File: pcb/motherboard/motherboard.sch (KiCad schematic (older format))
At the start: 37 parts, among them J1 -, J10 PSU, J11 RESET-SW, J14 EXT, J15 EXT-PW, J16 EXT-I2C, J6 PSU-SIG, J7 ICSP-1, J8 FRONT PANEL, SW1 RESET, U1 ATMEGA2560-16AU, Y2 16.00 MHz

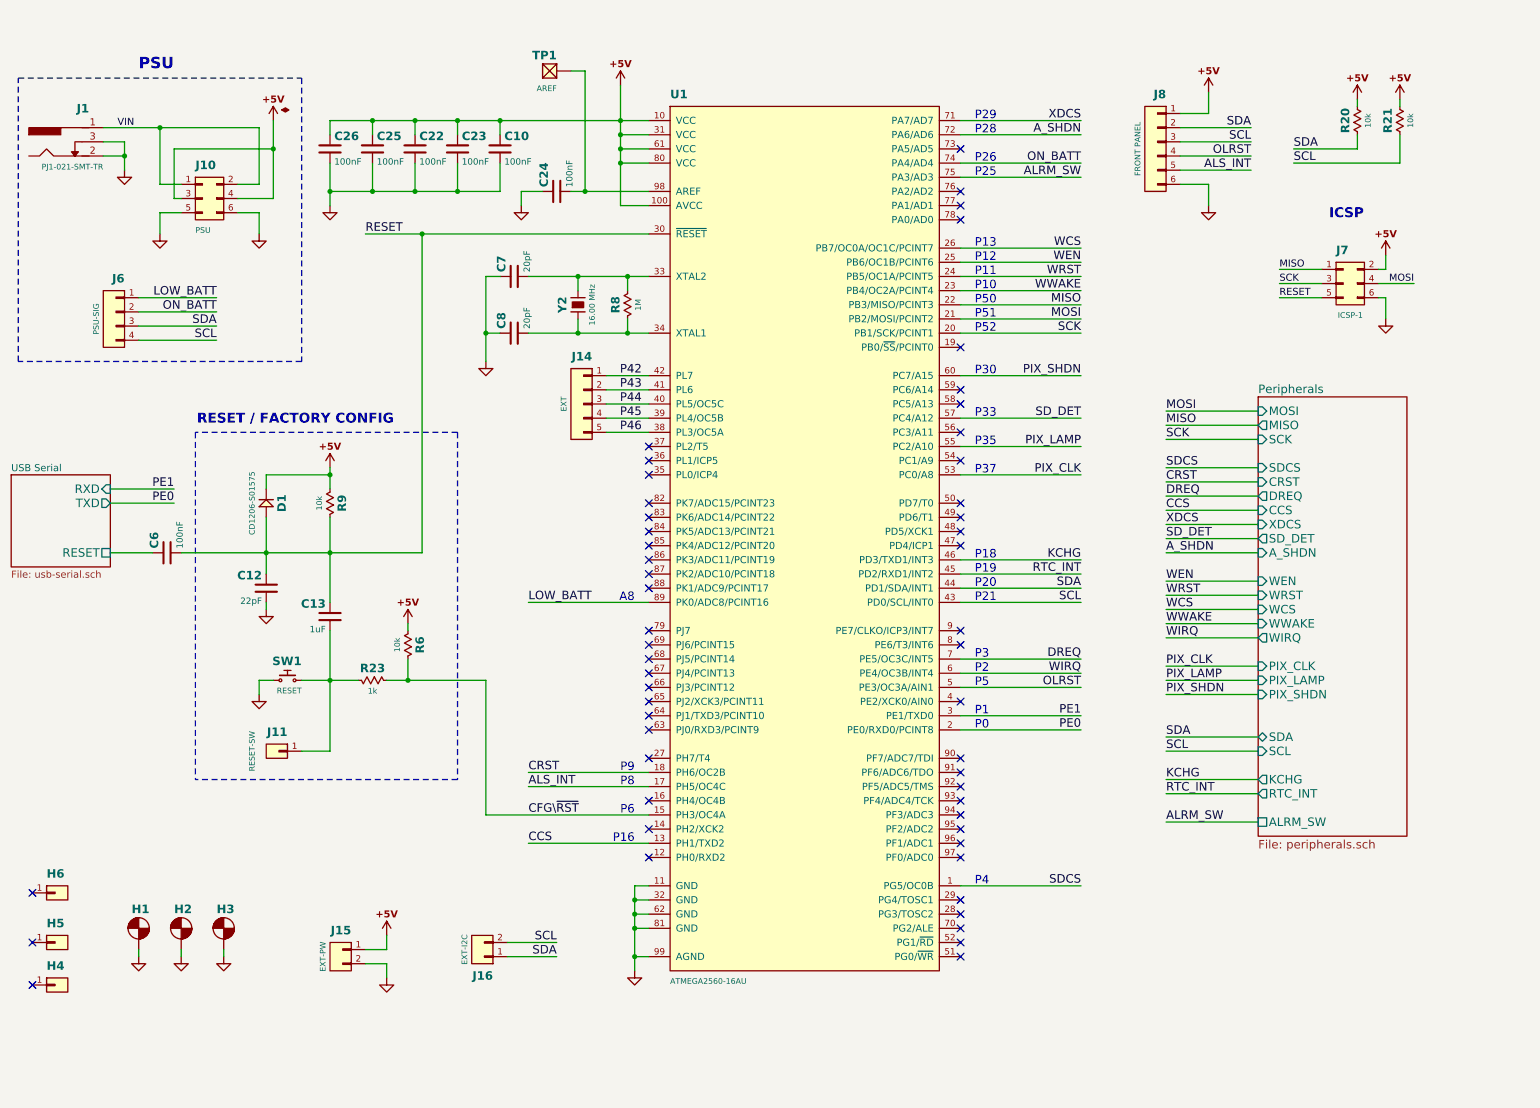
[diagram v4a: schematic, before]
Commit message: Replaced battery holder for Harwin S8411-45R
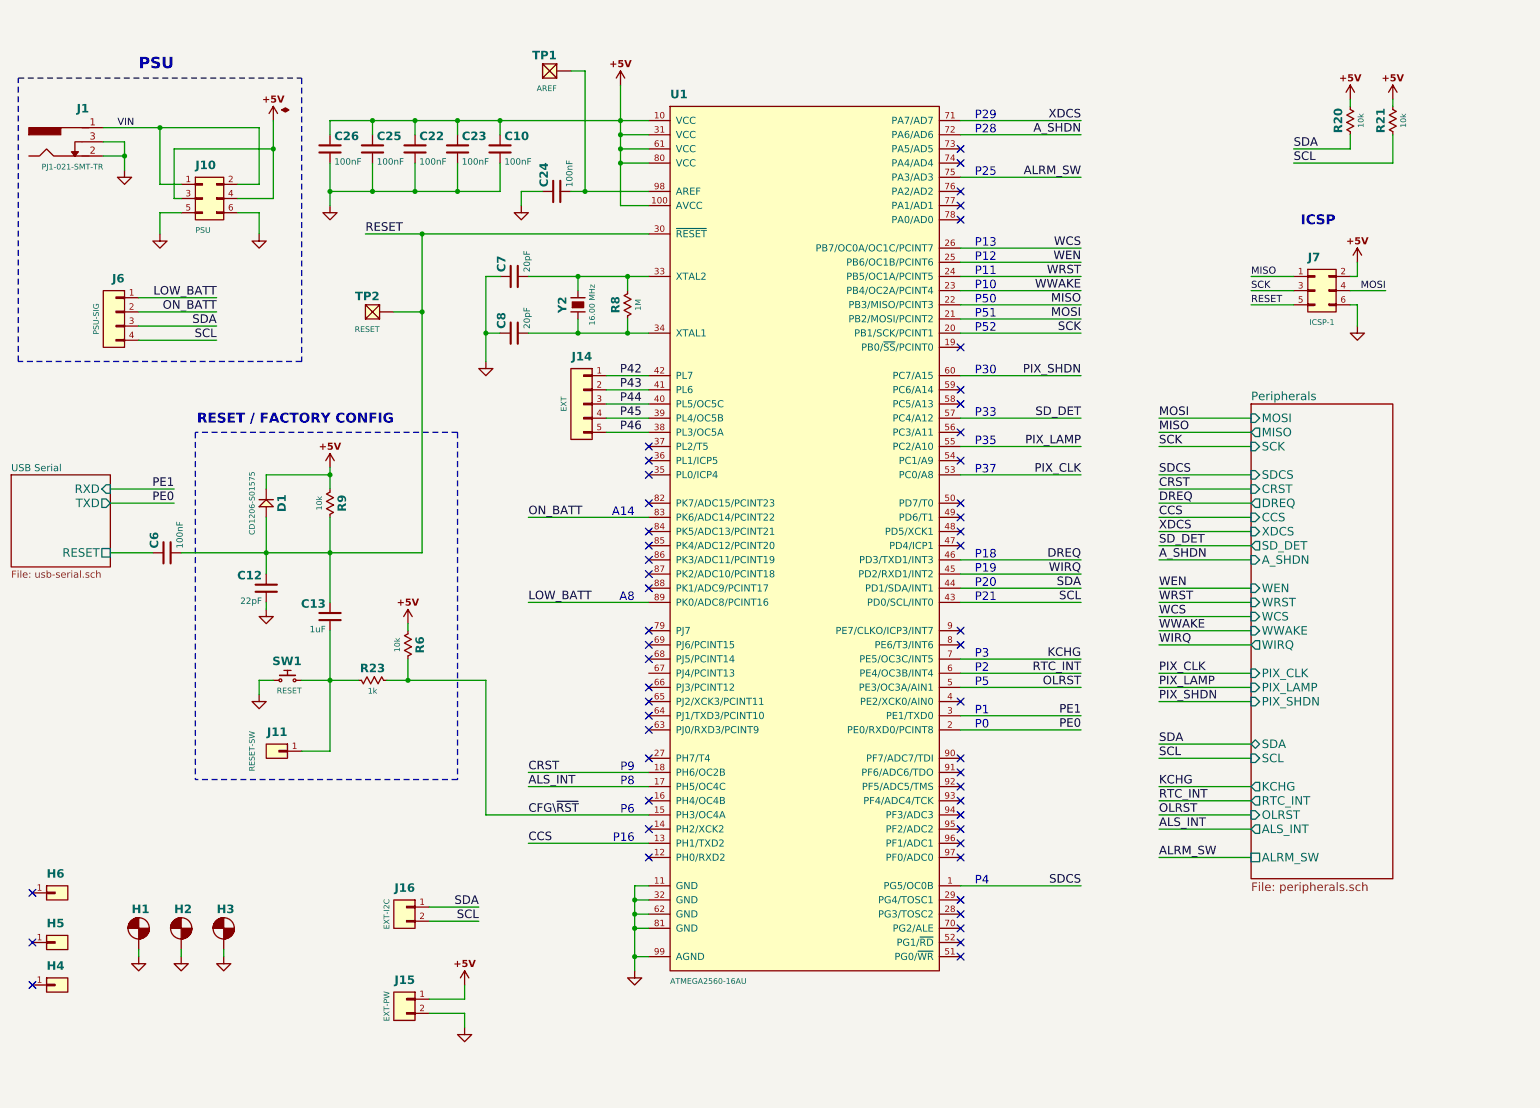
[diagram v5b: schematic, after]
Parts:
- removed J8: FRONT PANEL, conn-wire-pads:WP-50mil-1x06, symbol connectors:HEADER-1x06
- added TP2: RESET, conn-wire-pads:TEST-POINT-50, symbol connectors:TEST-POINT
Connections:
- net DREQ: now also U1.46 (PD3/TXD1/INT3); no longer U1.7 (PE5/OC3C/INT5)
- net KCHG: now also U1.7 (PE5/OC3C/INT5); no longer U1.46 (PD3/TXD1/INT3)
- net ON_BATT: now also U1.83 (PK6/ADC14/PCINT22); no longer U1.74 (PA4/AD4)
- net RESET: now also TP2.1 (P1)
- net RTC_INT: now also U1.6 (PE4/OC3B/INT4); no longer U1.45 (PD2/RXD1/INT2)
- net WIRQ: now also U1.45 (PD2/RXD1/INT2); no longer U1.6 (PE4/OC3B/INT4)
- no-connect marks 54 -> 53
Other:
- note added: "A14"
- note removed: "P26"
- moved on the sheet: J15, J16, J7, R20, R21

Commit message: Fix: Wrong footprint for R20-22 and C14
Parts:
- J7: value ICSP-1 -> ICSP
- R20, R21: footprint smt:C-0603 -> smt:R-0603
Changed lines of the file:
@@
 P 9800 2450
 F 0 "J7" H 9700 2650 60  0000 L BNB
-F 1 "ICSP-1" H 9800 2250 40  0000 C TNN
+F 1 "ICSP" H 9800 2250 40  0000 C TNN
 F 2 "conn-header:HDR-M-2x03" H 9800 1250 60  0001 C CNN
 F 3 "" H 9800 1250 60  0001 C CNN
@@
 F 0 "R20" H 10000 1335 60  0000 C CNB
 F 1 "10k" H 10000 1175 40  0000 C CNN
-F 2 "smt:C-0603" H 10000 1110 40  0001 C CNN
+F 2 "smt:R-0603" H 10000 1110 40  0001 C CNN
 F 3 "" H 10000 1350 60  0000 C CNN
 F 4 "-" H 10000 1410 45  0001 C CNN "Part"
@@
 F 0 "R21" H 10300 1335 60  0000 C CNB
 F 1 "10k" H 10300 1175 40  0000 C CNN
-F 2 "smt:C-0603" H 10300 1110 40  0001 C CNN
+F 2 "smt:R-0603" H 10300 1110 40  0001 C CNN
 F 3 "" H 10300 1350 60  0000 C CNN
 F 4 "-" H 10300 1410 45  0001 C CNN "Part"

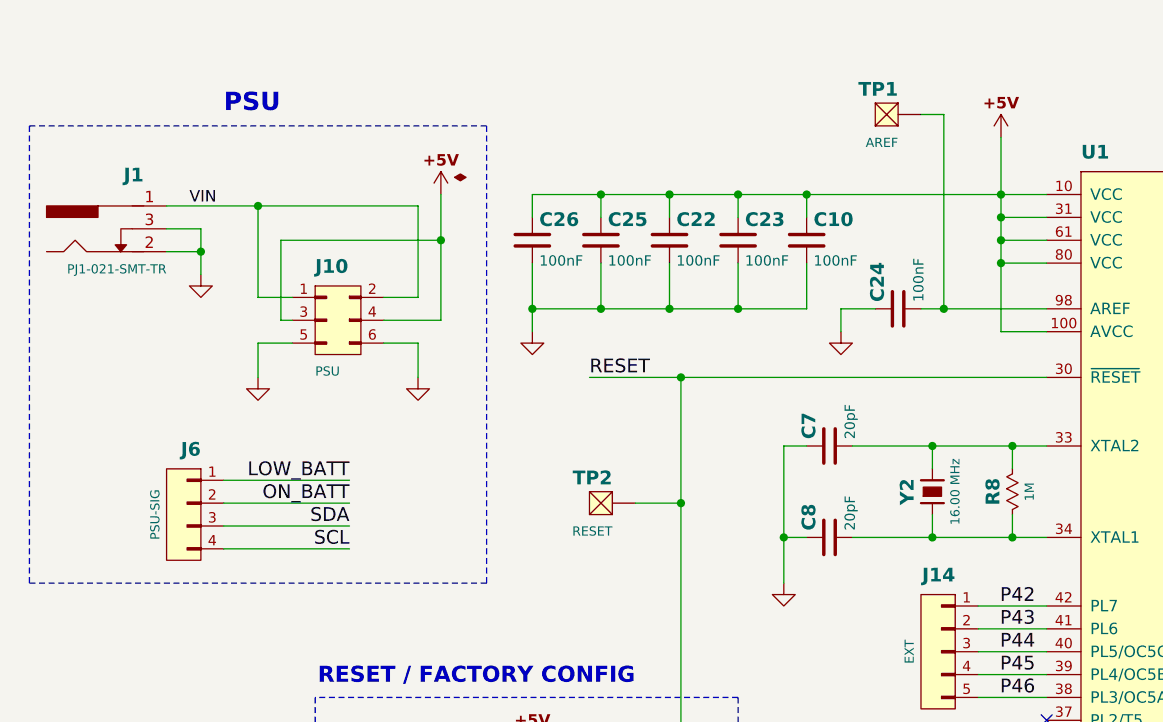
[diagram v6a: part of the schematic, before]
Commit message: Corrected solder mask clearance
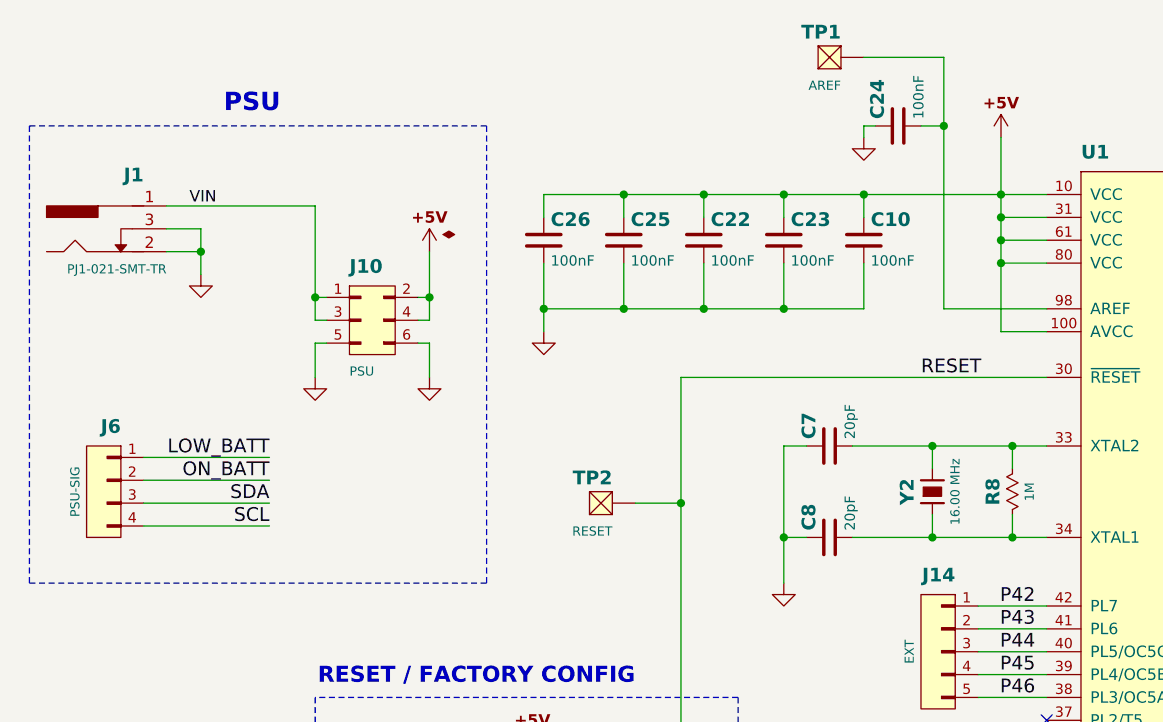
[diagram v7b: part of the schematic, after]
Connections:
- net +5V: now also J10.2 (P2); no longer J10.3 (P3)
- net VIN: now also J10.3 (P3); no longer J10.2 (P2)
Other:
- moved on the sheet: C10, C22, C23, C24, C25, C26, J10, J6, TP1

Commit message: PSU board schematics/layout
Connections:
- net LOW_BATT renamed SYSOFF
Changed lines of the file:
@@
 	5050 4650 4200 4650
 Text Label 4200 4650 0    60   ~ 0
-LOW_BATT
+SYSOFF
 Wire Wire Line
 	2800 4300 3450 4300
@@
 ON_BATT
 Text Label 1650 2400 2    60   ~ 0
-LOW_BATT
+SYSOFF
 Wire Wire Line
 	1100 2500 1650 2500
